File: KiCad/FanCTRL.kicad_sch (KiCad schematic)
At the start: 20 parts, among them J201 Conn_01x04_Pin, J202 Conn_01x04_Pin, Q301 BSS138, Q401 BSS138, U201 AP2112K-3.3, U202 STM32G030F6Px

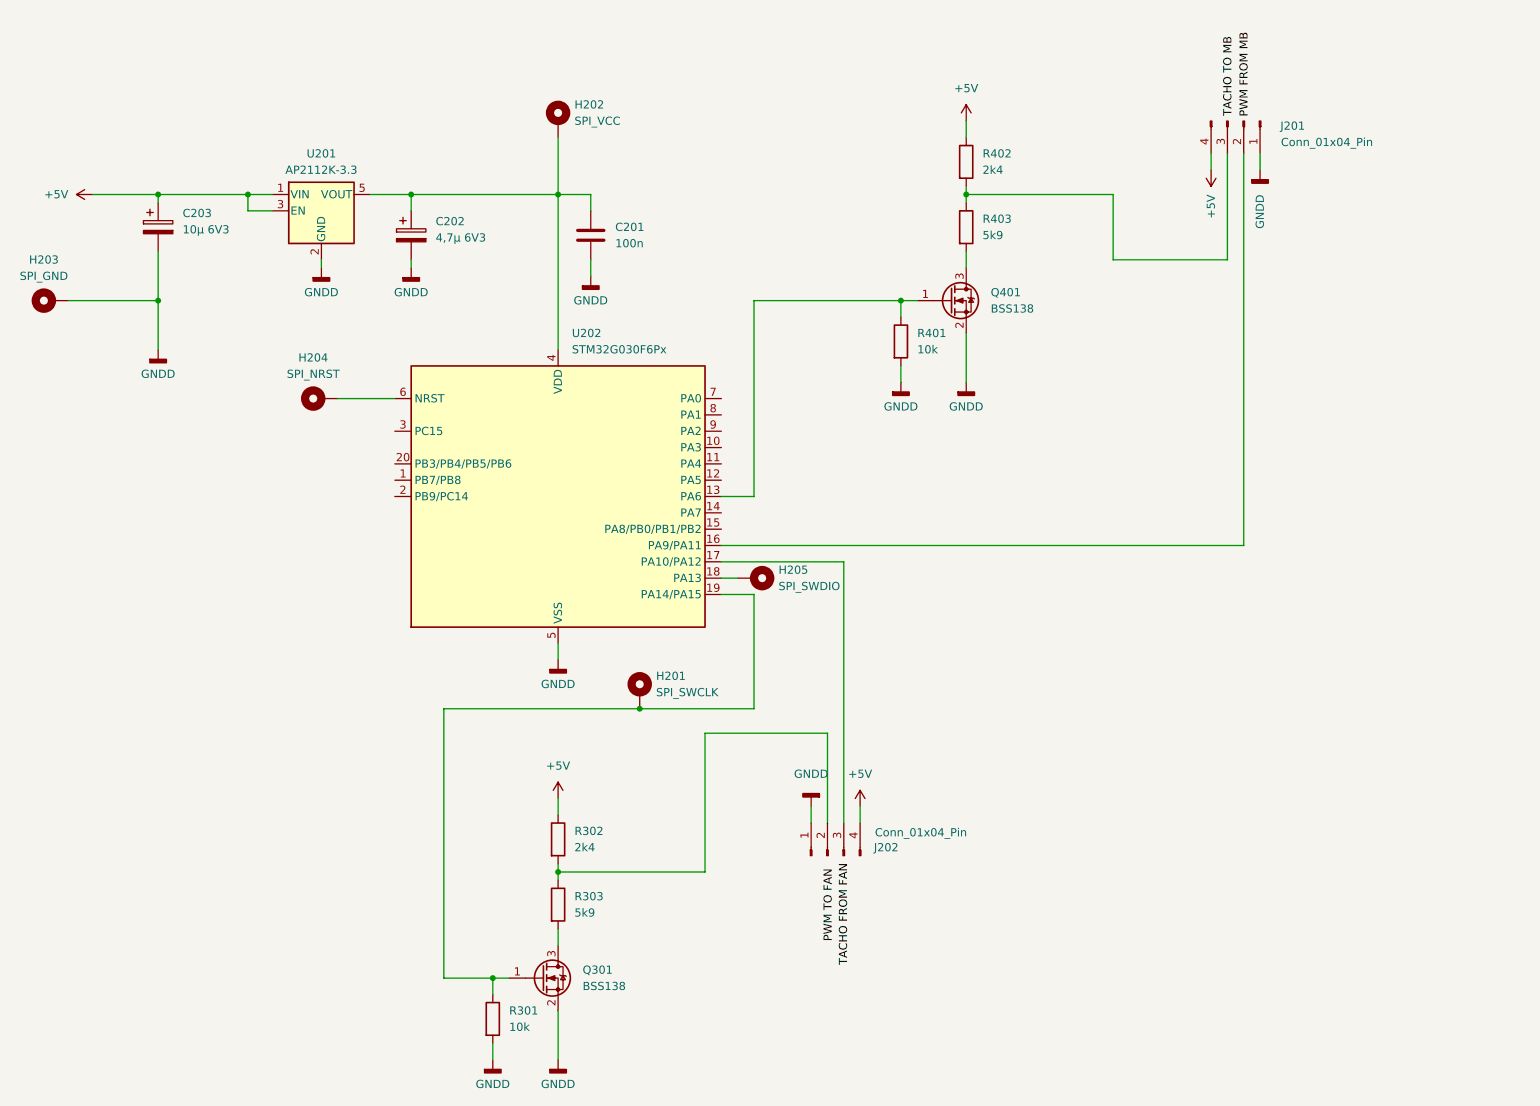
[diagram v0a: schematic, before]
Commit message: Added and edited some Texts in Schematic and Board
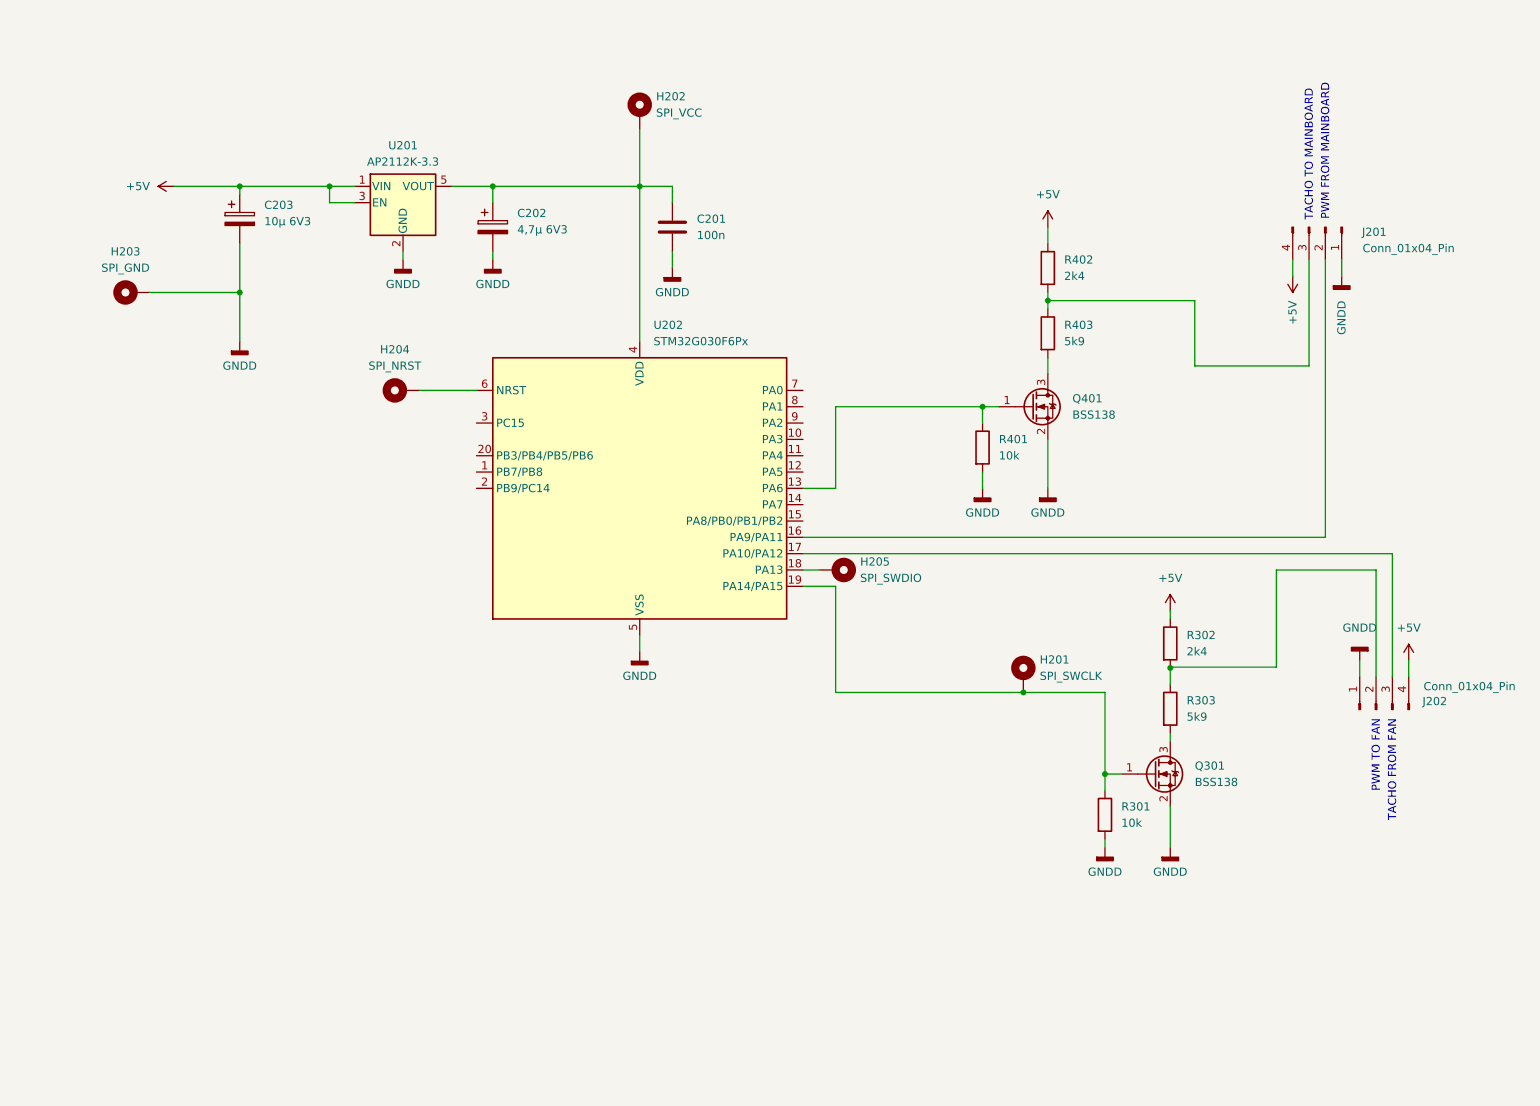
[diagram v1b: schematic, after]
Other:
- note added: "PWM FROM MAINBOARD"
- note added: "PWM TO FAN"
- note added: "TACHO FROM FAN"
- note added: "TACHO TO MAINBOARD"
- company: (none) -> Code99 www.code99.it
- title: (none) -> FanCTRL - Prod. ID 7CP2X9NW
- moved on the sheet: C201, C202, C203, H201, H202, H203, H204, H205, J201, J202, Q301, Q401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
